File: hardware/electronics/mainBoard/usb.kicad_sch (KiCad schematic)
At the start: 60 parts, among them J1 USB_C_Receptacle_USB2.0, U13 TPS25751D, U3 TUSB4041I-Q1

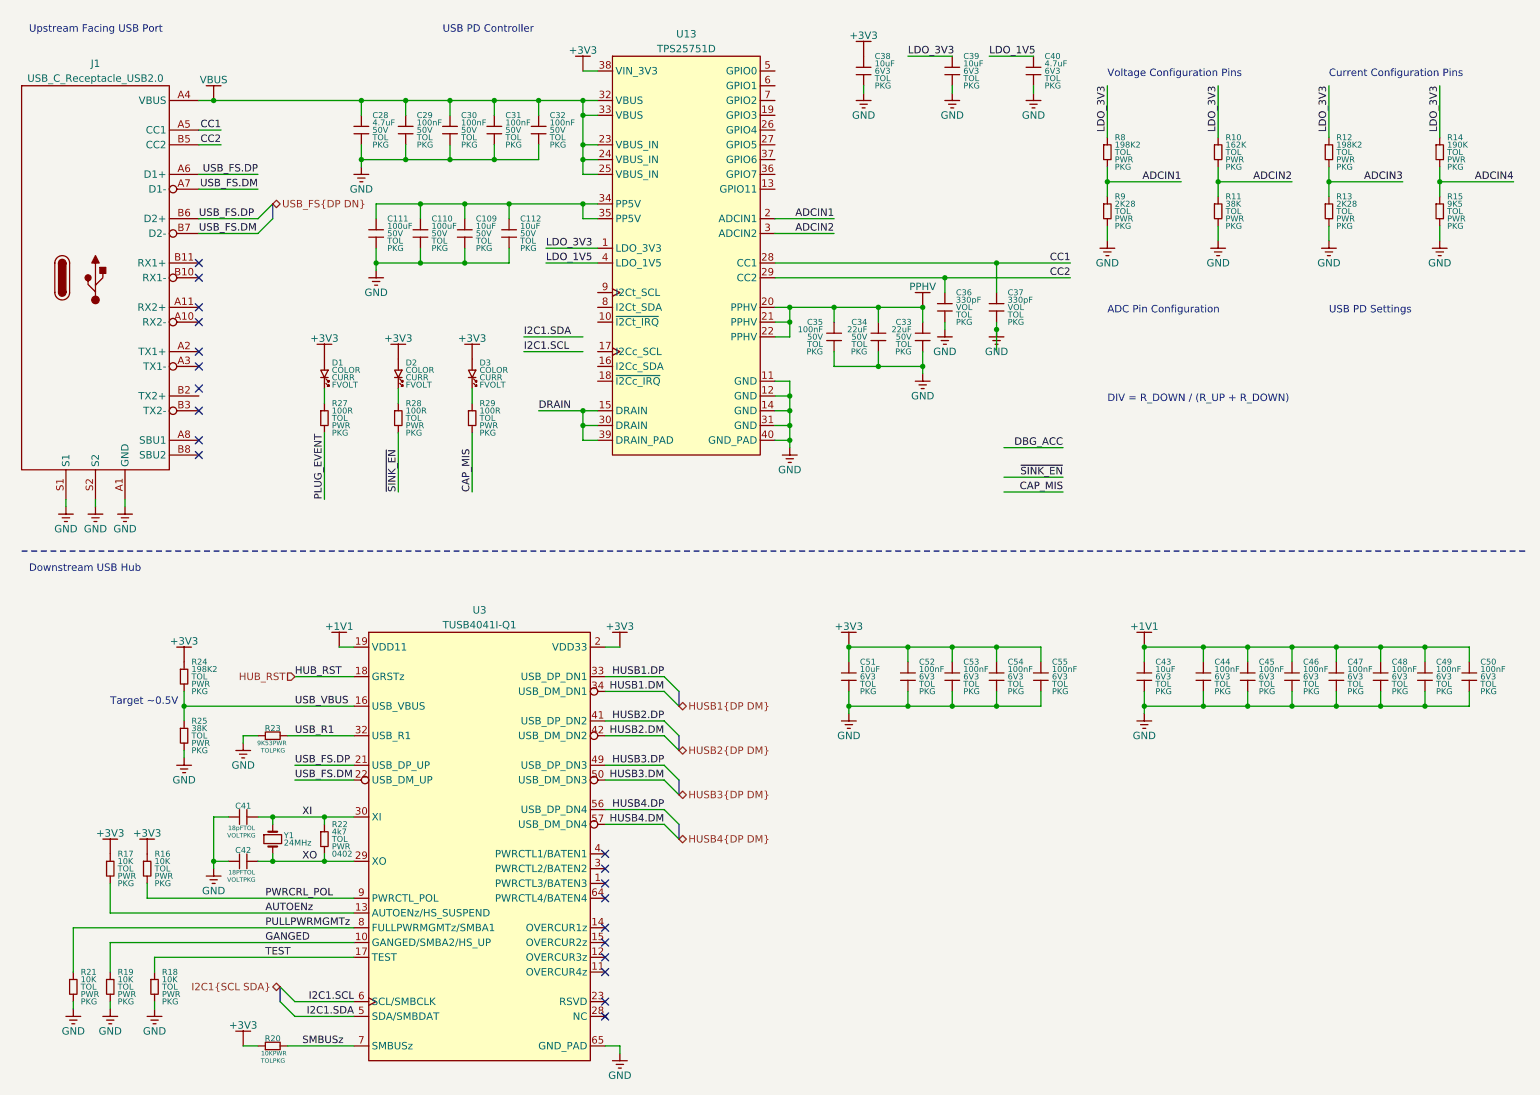
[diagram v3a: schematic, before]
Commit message: finished(?) USB PD
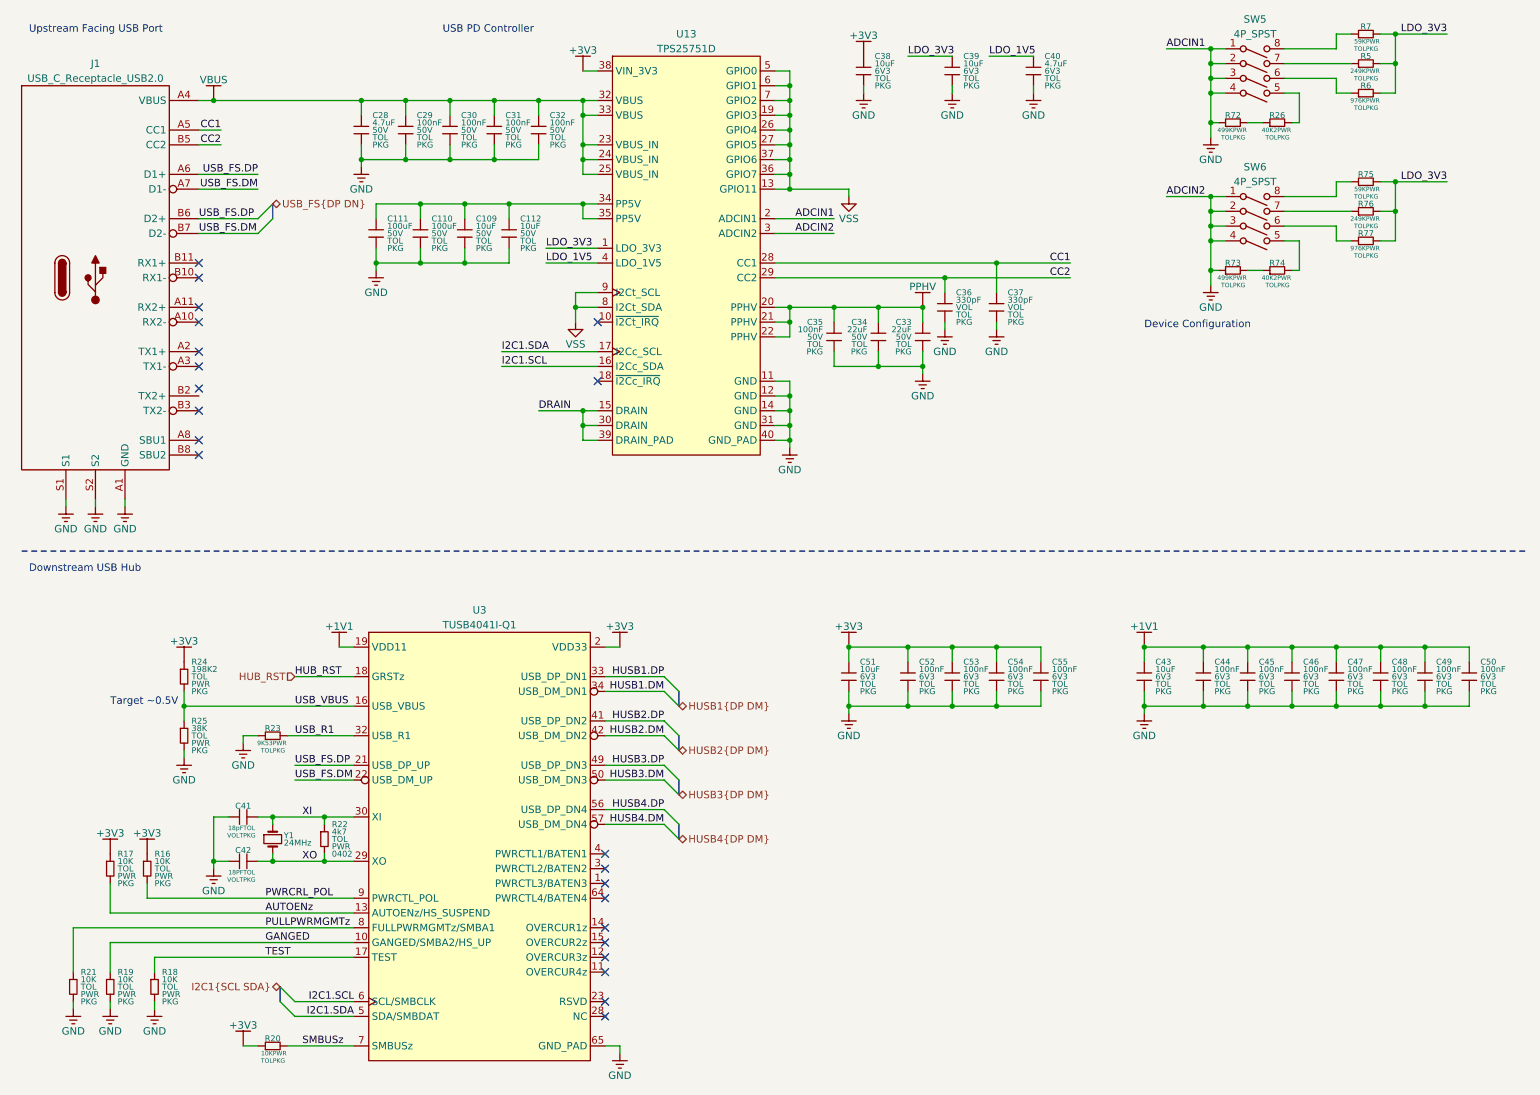
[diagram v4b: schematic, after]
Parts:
- removed D1, D2, D3: ~, symbol lib_sch:LED
- removed R10: 162K, symbol lib_sch:R
- removed R11: 38K, symbol lib_sch:R
- removed R12, R8: 198K2, symbol lib_sch:R
- removed R13, R9: 2K28, symbol lib_sch:R
- removed R14: 190K, symbol lib_sch:R
- removed R15: 9K5, symbol lib_sch:R
- removed R27, R28, R29: 100R, symbol lib_sch:R
- added R26, R74: 40K2, symbol lib_sch:R_horizontal
- added R5, R76: 249K, symbol lib_sch:R_horizontal
- added R6, R77: 976K, symbol lib_sch:R_horizontal
- added R7, R75: 59K, symbol lib_sch:R_horizontal
- added R72, R73: 499K, symbol lib_sch:R_horizontal
- added SW5, SW6: 4P_SPST, symbol .DS-Switches:4P_SPST
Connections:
- net ADCIN1 is gone; now on net GND: U13.2 (ADCIN1)
- net ADCIN2 is gone; now on net GND: U13.3 (ADCIN2)
- net GND: now also R72.1, R73.1, SW5.1, SW5.2, SW5.3, SW5.4, SW6.1, SW6.2, SW6.3, SW6.4
- net I2C1.SCL: now also U13.16 (I2Cc_SDA)
- net I2C1.SDA: now also U13.17 (I2Cc_SCL)
- net LDO_3V3: now also R5.2, R6.2, R7.2, R75.2, R76.2, R77.2
- net VSS: now reaches U13.13 (GPIO11)
- net VSS: now also U13.19 (GPIO3), U13.26 (GPIO4), U13.27 (GPIO5), U13.36 (GPIO7), U13.37 (GPIO6), U13.5 (GPIO0), U13.6 (GPIO1), U13.7 (GPIO2), U13.8 (I2Ct_SDA), U13.9 (I2Ct_SCL)
- new net: R26.1, R72.2
- new net: R26.2, SW5.5
- new net: R76.1, SW6.7
- new net: R75.1, SW6.8
- new net: R73.2, R74.1
- new net: R74.2, SW6.5
- new net: R77.1, SW6.6
- new net: R5.1, SW5.7
- new net: R6.1, SW5.6
- new net: R7.1, SW5.8
- no-connect marks 20 -> 22
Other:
- note added: "Device Configuration"
- note removed: "ADC Pin Configuration"
- note removed: "Current Configuration Pins"
- note removed: "DIV = R_DOWN / (R_UP + R_DOWN)"
- note removed: "USB PD Settings"
- note removed: "Voltage Configuration Pins"

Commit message: moved PD to EPS
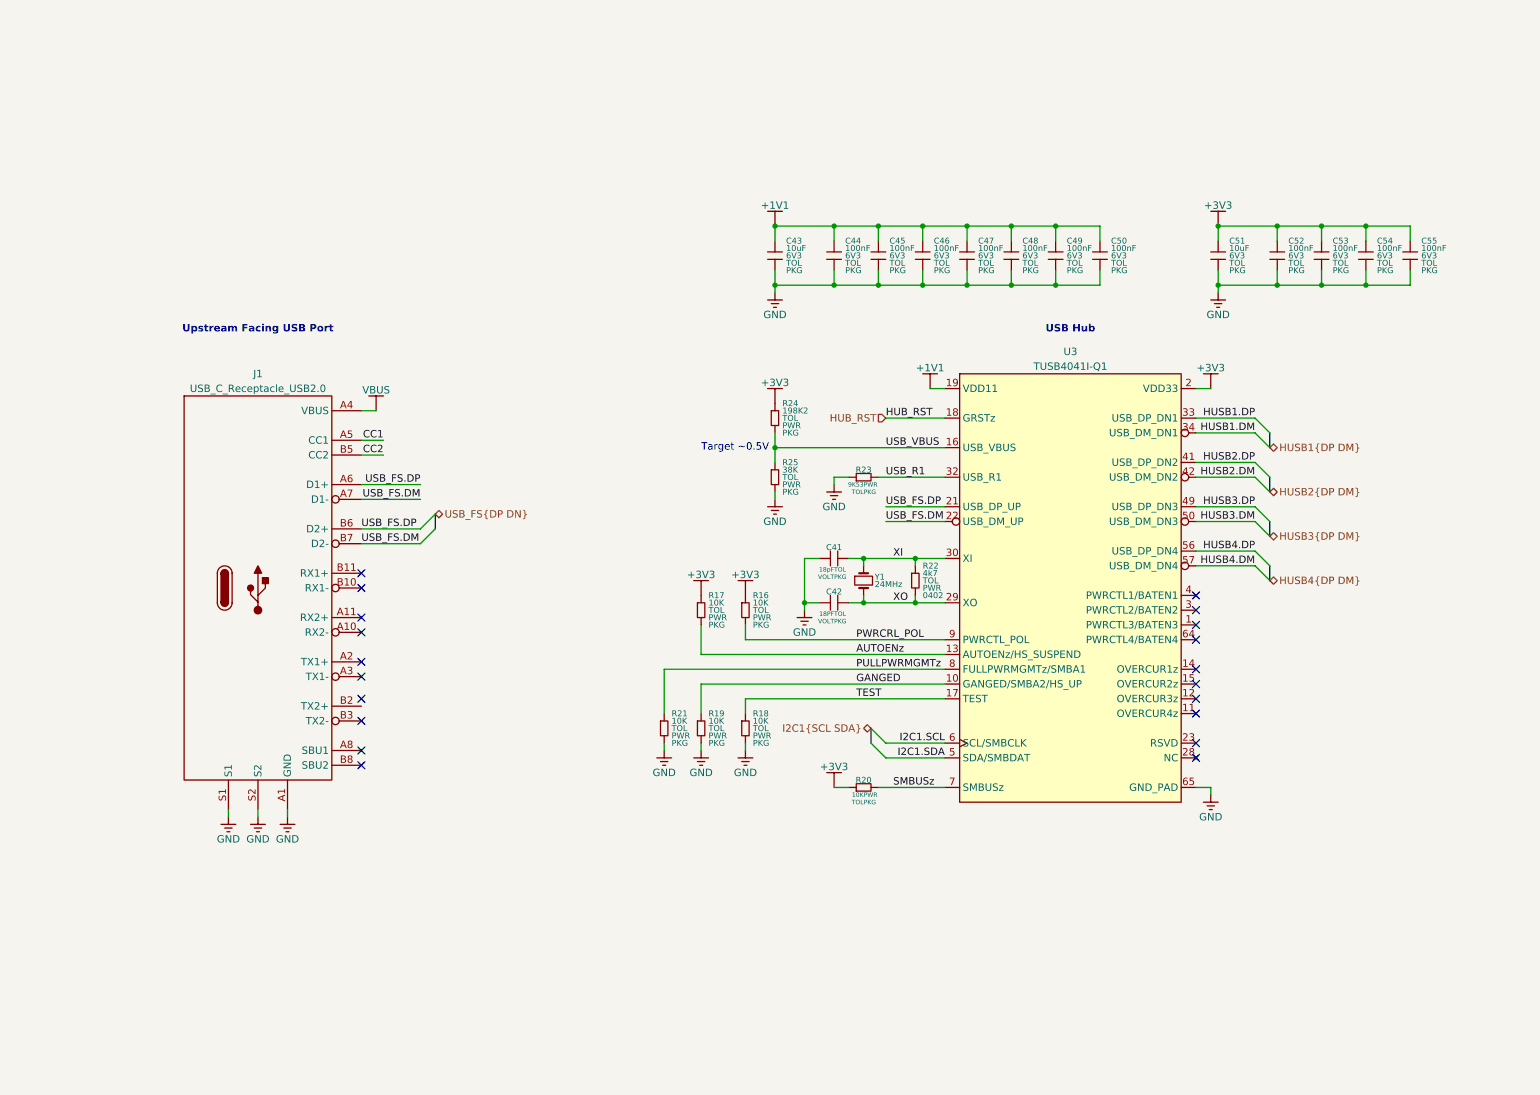
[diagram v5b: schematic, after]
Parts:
- removed C109, C112, C38, C39: 10uF, symbol lib_sch:C
- removed C110, C111: 100uF, symbol lib_sch:C
- removed C28, C40: 4.7uF, symbol lib_sch:C
- removed C29, C30, C31, C32, C35: 100nF, symbol lib_sch:C
- removed C33, C34: 22uF, symbol lib_sch:C
- removed C36, C37: 330pF, symbol lib_sch:C
- removed R26, R74: 40K2, symbol lib_sch:R_horizontal
- removed R5, R76: 249K, symbol lib_sch:R_horizontal
- removed R6, R77: 976K, symbol lib_sch:R_horizontal
- removed R7, R75: 59K, symbol lib_sch:R_horizontal
- removed R72, R73: 499K, symbol lib_sch:R_horizontal
- removed SW5, SW6: 4P_SPST, symbol .DS-Switches:4P_SPST
- removed U13: TPS25751D, symbol .DS-PMIC:TPS25751D
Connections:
- no-connect marks 22 -> 20
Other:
- note added: "USB Hub"
- note removed: "Device Configuration"
- note removed: "Downstream USB Hub"
- note removed: "USB PD Controller"
- moved on the sheet: C41, C42, C43, C44, C45, C46, C47, C48, C49, C50, C51, C52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

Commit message: moved PD to new sheet
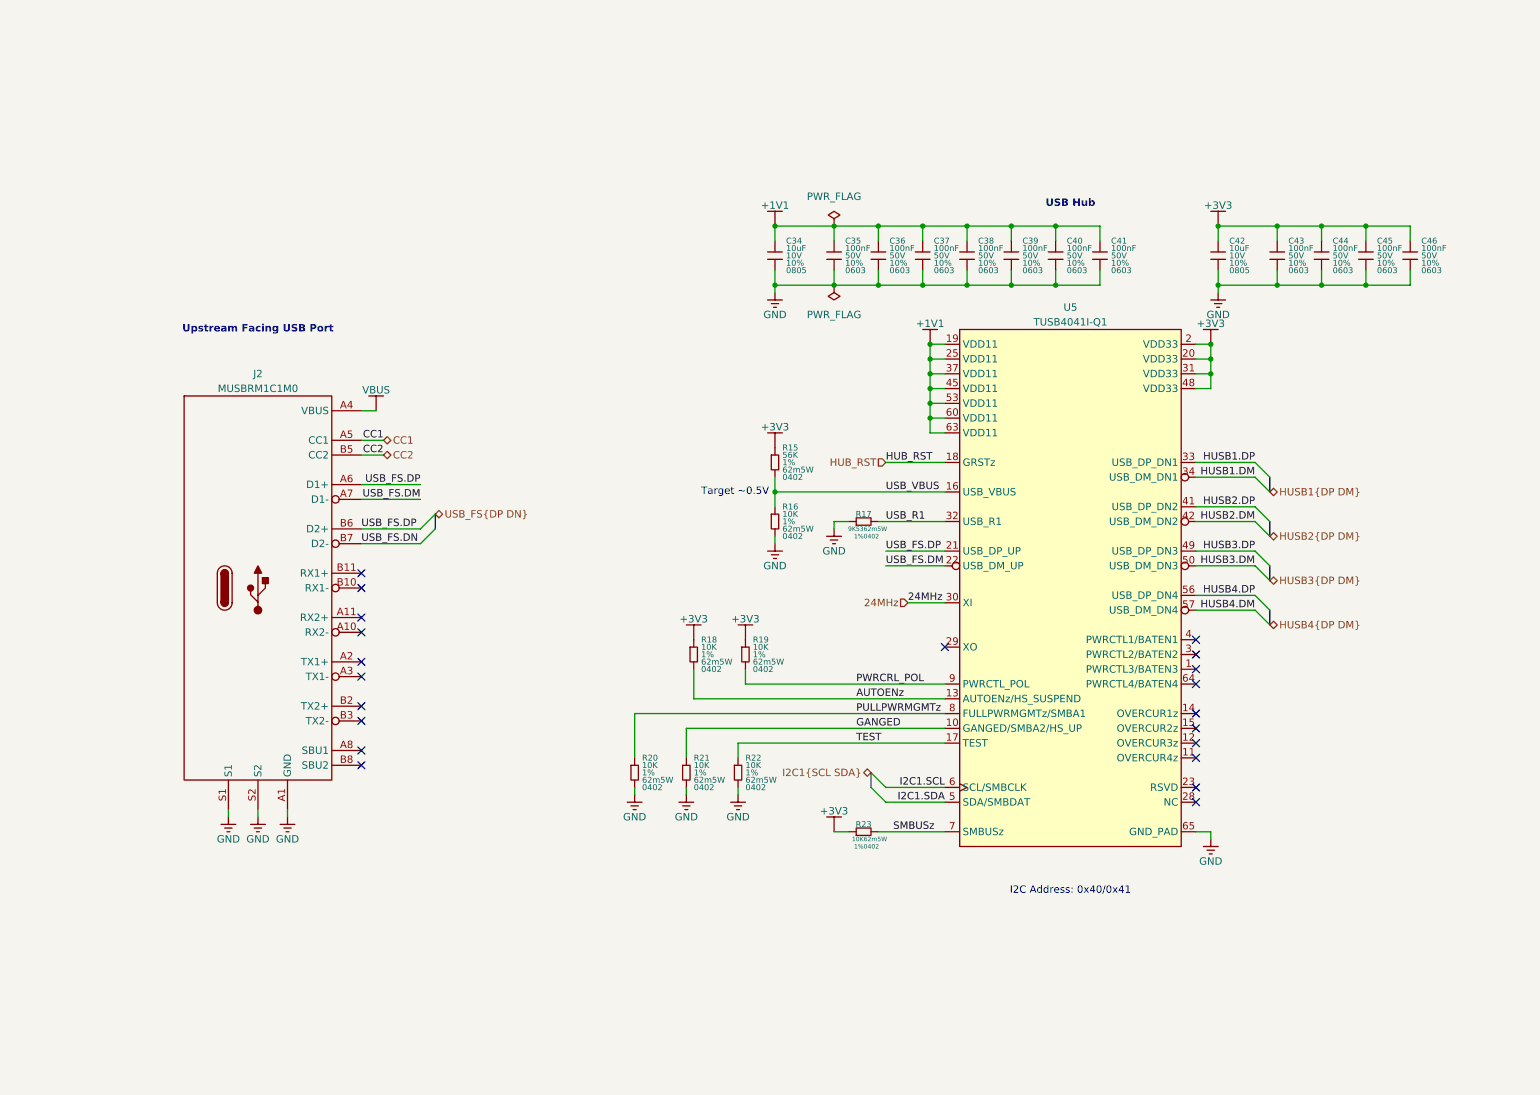
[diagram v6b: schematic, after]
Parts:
- removed C41: 18pF, symbol lib_sch:C_horizontal
- removed C42: 18PF, symbol lib_sch:C_horizontal
- removed C47, C48, C49, C50, C52, C53, C54, C55: 100nF, symbol lib_sch:C
- removed C51: 10uF, symbol lib_sch:C
- removed R17: 10K, symbol lib_sch:R
- removed R20: 10K, symbol lib_sch:R_horizontal
- removed R24: 198K2, symbol lib_sch:R
- removed R25: 38K, symbol lib_sch:R
- removed Y1: ~, symbol lib_sch:crystal_small
- added C34, C42: 10uF, symbol lib_sch:C
- added C35, C36, C37, C38, C39, C40, C41: 100nF, symbol lib_sch:C
- added R15: 56K, symbol lib_sch:R
- added R20: 10K, symbol lib_sch:R
- added R23: 10K, symbol lib_sch:R_horizontal
- C43: value 10uF -> 100nF; DKPN (none) -> 478-KAM15AR71H104KTCT-ND; MPN (none) -> 06035C104K4T2A; Manufacturer (none) -> KYOCERA AVX; Package PKG -> 0603; Tolerance TOL -> 10%; Voltage Rating 6V3 -> 50V
- C44, C45, C46: DKPN (none) -> 478-KAM15AR71H104KTCT-ND; MPN (none) -> 06035C104K4T2A; Manufacturer (none) -> KYOCERA AVX; Package PKG -> 0603; Tolerance TOL -> 10%; Voltage Rating 6V3 -> 50V
- J2: renamed from J1; value USB_C_Receptacle_USB2.0 -> MUSBRM1C1M0; DKPN (none) -> MUSBRM1C1M0-ND; MPN (none) -> MUSBRM1C1M0; Manufacturer (none) -> Amphenol ICC (Commercial Products)
- R16, R18, R19, R21: DKPN (none) -> 541-10.0KLCT-ND; MPN (none) -> CRCW040210K0FKED; Manufacturer (none) -> Vishay Dale; Package PKG -> 0402; Power Rating PWR -> 62m5W; Tolerance TOL -> 1%
- R17: renamed from R23; DKPN (none) -> 541-9.53KLCT-ND; MPN (none) -> CRCW04029K53FKED; Manufacturer (none) -> Vishay Dale; Package PKG -> 0402; Power Rating PWR -> 62m5W; Tolerance TOL -> 1%
- R22: value 4k7 -> 10K; DKPN (none) -> 541-10.0KLCT-ND; MPN (none) -> CRCW040210K0FKED; Manufacturer (none) -> Vishay Dale; Power Rating PWR -> 62m5W; Tolerance TOL -> 1%
- renumbered U3 to U5
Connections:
- net +1V1: now also C34.1, C35.1, C36.1, C37.1, C38.1, C39.1, C40.1, C41.1; no longer C43.1, C44.1, C45.1, C46.1
- net +3V3: now also C43.1, C44.1, C45.1, C46.1, R18.1, R19.1, C42.1, R15.1, R23.1; no longer R16.1
- net AUTOENz: now also R18.2
- net GANGED: now also R21.1; no longer R19.1
- net GND: now also R16.2, R22.2, C34.2, C35.2, C36.2, C37.2, C38.2, C39.2, C40.2, C41.2, C42.2, R20.2; no longer R18.2, R19.2
- net PULLPWRMGMTz: now also R20.1; no longer R21.1
- net PWRCRL_POL: now also R19.2; no longer R16.2
- net SMBUSz: now also R23.2
- net TEST: now also R22.1; no longer R18.1
- net USB_FS.DM: no longer J2.B7 (D2-)
- net USB_VBUS: now also R16.1, R15.2
- net XI renamed 24MHz
- net 24MHz: no longer R22.1
- net XO: no longer names the net of U5.29 (XO)
- net XO: no longer R22.2
- new net USB_FS.DN: J2.B7 (D2-)
- no-connect marks 20 -> 21
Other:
- note added: "I2C Address: 0x40/0x41"
- moved on the sheet: R17
